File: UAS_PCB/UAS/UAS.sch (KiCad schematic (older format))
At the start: 18 parts, among them J1 SM04B-GHS-TB(LF)(SN)-, J2 SM07B-GHS-TB(LF)(SN), J3 SM04B-GHS-TB(LF)(SN)-, J4 SM08B-GHS-TB(LF)(SN), J5 SM08B-GHS-TB(LF)(SN), J6 SM04B-GHS-TB(LF)(SN)-, J7 SM04B-GHS-TB(LF)(SN)-, J8 SM07B-GHS-TB(LF)(SN), U10 UAS-rescue_7.5V-2.4A-Converte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, U11 JST-3-Pin, U12 Signal-Pad, U13 Signal-Pad, U2 5A-5V-Converter, U3 500mA-5V-Converter, U4 12V-StepUp-Converter, U5 TB6612FNG-Dual-Motor-Driver, U7 UAS-rescue_JST-4-Pin-UAS-cache, U9 JST-3-Pin

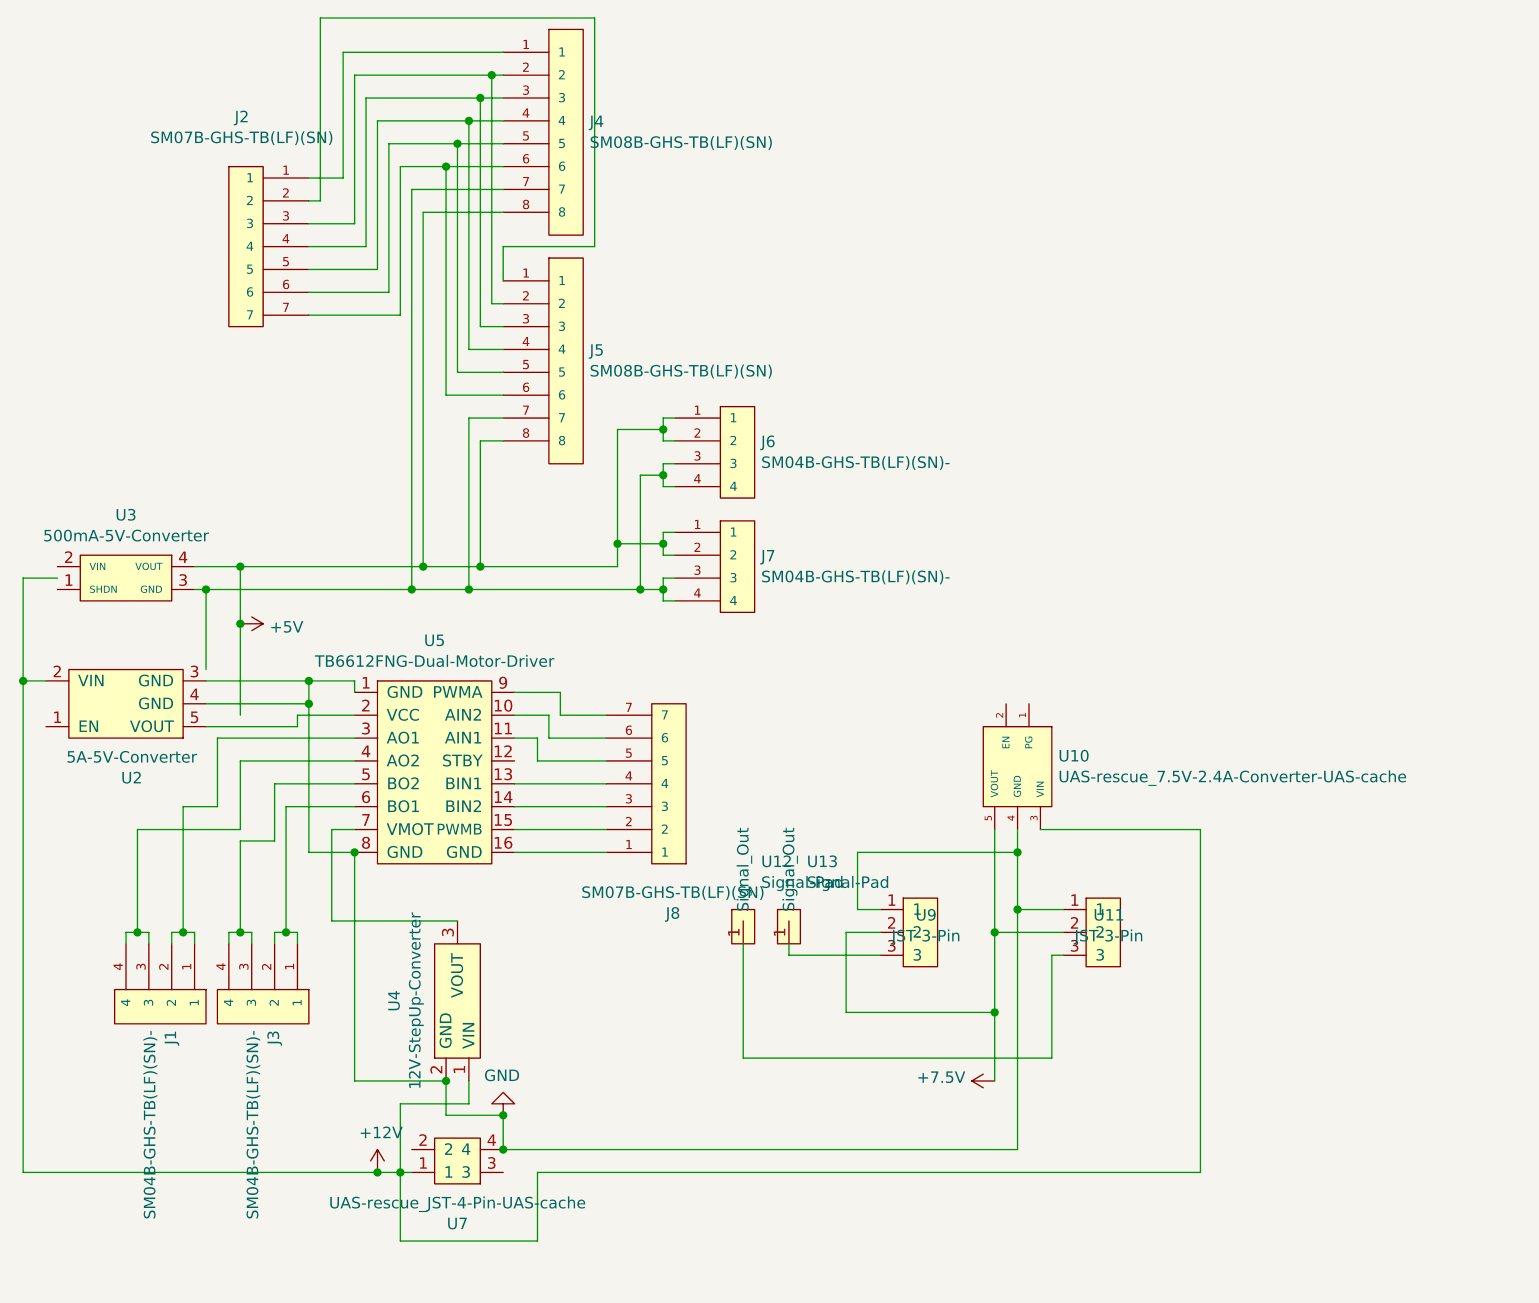
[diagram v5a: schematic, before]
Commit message: 12V Converter Added
read title
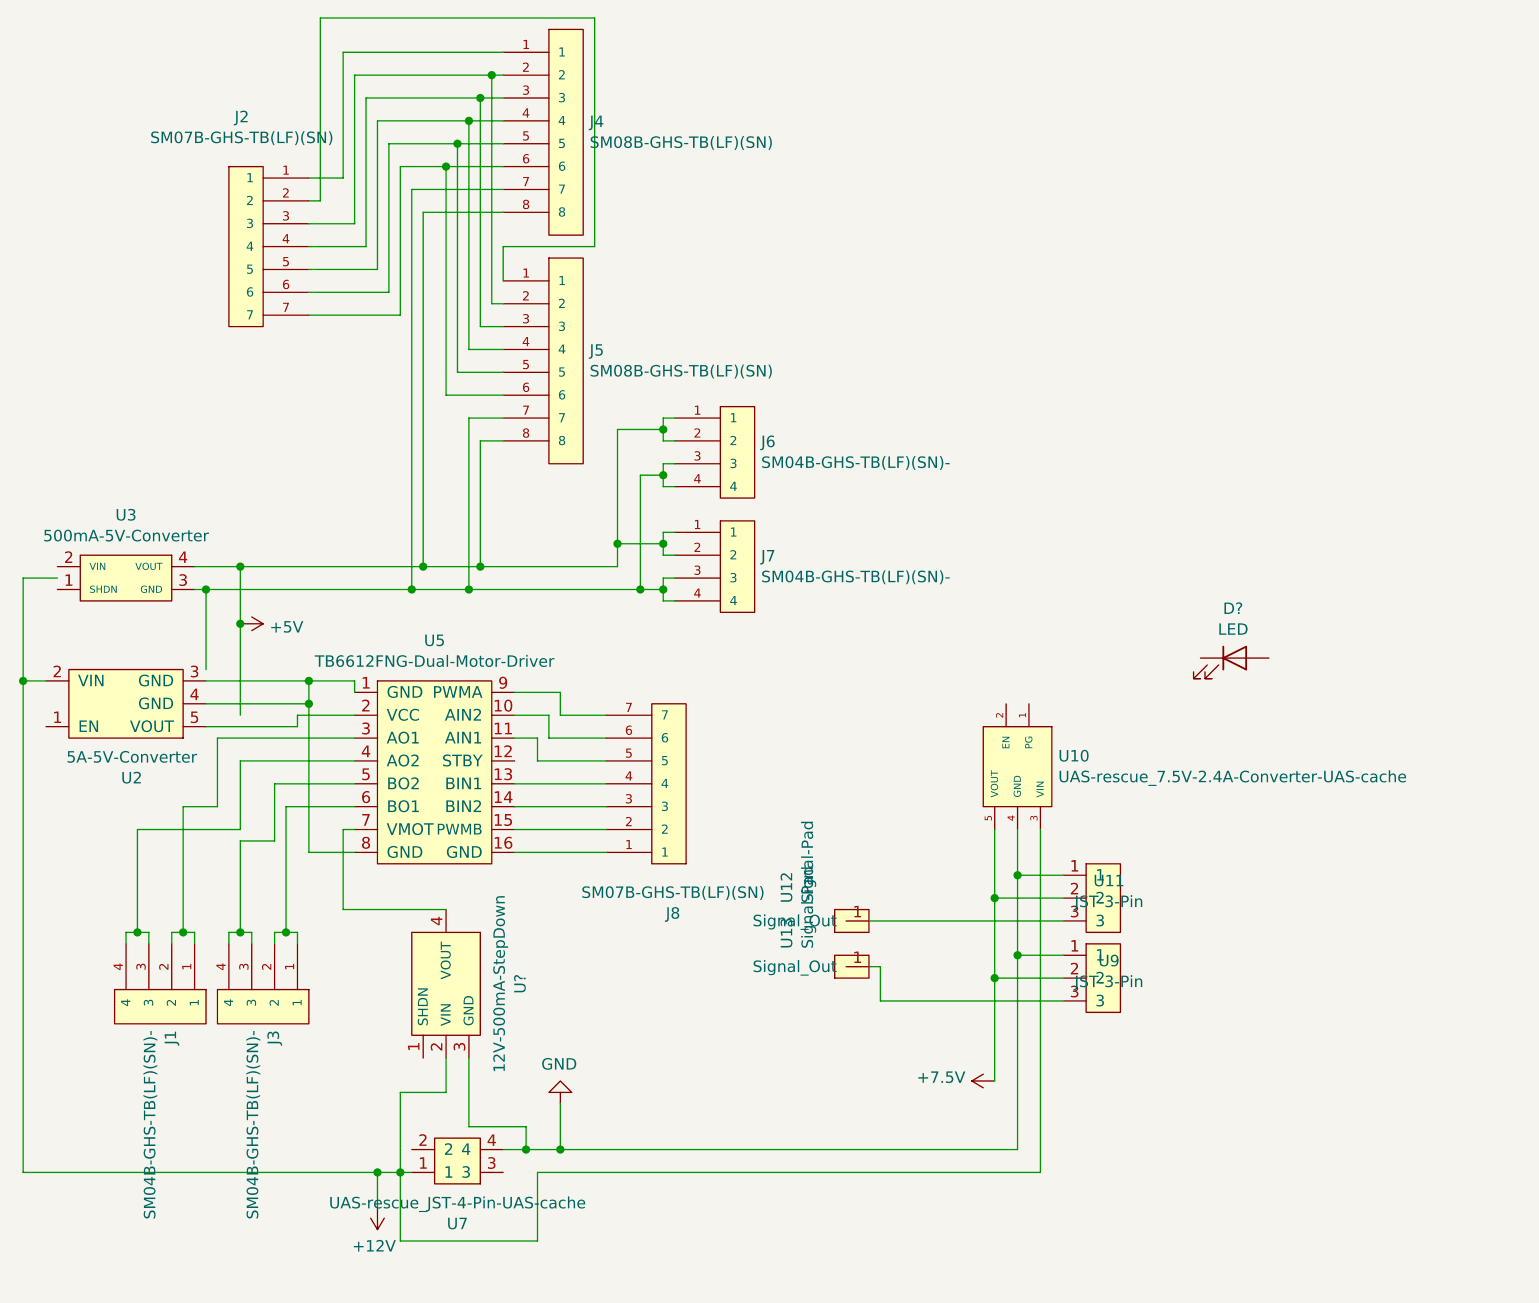
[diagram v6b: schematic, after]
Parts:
- removed U4: 12V-StepUp-Converter, UAS:Pololu_12V_Step_Up_Voltage_Regulator_SMT, symbol UAS-rescue:12V-StepUp-Converter-UAS-cache
- added D?: LED, UAS:Indicator-LED, symbol Device:LED
- added U?: 12V-500mA-StepDown, UAS:12V-500mA-StepDown, symbol UAS:12V-500mA-StepDown
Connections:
- net +12V: now also U?.2 (VIN)
- net GND: now also U?.3 (GND); no longer U2.3 (GND), U2.4 (GND), U5.1 (GND), U5.8 (GND)
- net at U5.7 (VMOT): now also U?.4 (VOUT)
- new net: U2.3 (GND), U2.4 (GND), U5.1 (GND), U5.8 (GND)
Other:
- moved on the sheet: U11, U12, U13, U9
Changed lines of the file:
@@
 $EndComp
-Wire Wire Line
-	3200 6300 3200 6150
-Wire Wire Line
-	3200 6150 2950 6150
-Wire Wire Line
-	2950 6150 2950 6000
-Wire Wire Line
-	2750 6400 2750 6100
-Wire Wire Line
-	3050 6100 3050 6000
-Wire Wire Line
-	2750 6100 3050 6100
-Wire Wire Line
-	3000 5300 2450 5300
-Wire Wire Line
-	2450 5300 2450 4900
-Wire Wire Line
-	2450 4900 2550 4900
-Wire Wire Line
-	2550 5000 2550 6000
-Wire Wire Line
-	2550 6000 2950 6000
-Connection ~ 2950 6000
 Wire Wire Line
 	1100 4250 1100 6400
-Wire Wire Line
-	1100 6400 2650 6400
 Connection ~ 1100 4250
 Connection ~ 2750 6400
@@
 Wire Wire Line
 	2350 5000 2550 5000
-Connection ~ 2550 5000
-Wire Wire Line
-	6250 6400 3350 6400
 Wire Wire Line
 	3350 6400 3350 6700
@@
 	2750 6700 2750 6400
 Wire Wire Line
-	3200 6300 5450 6300
-Connection ~ 3200 6300
-$Comp
-L UAS-rescue:Signal-Pad-UAS-cache U12
-U 1 1 60391DEE
-P 4250 5300
-F 0 "U12" H 4328 5559 50  0000 L CNN
-F 1 "Signal-Pad" H 4328 5468 50  0000 L CNN
-F 2 "UAS:Individual_Solder_Pad" H 4250 5300 50  0001 C CNN
-F 3 "" H 4250 5300 50  0001 C CNN
-	1    4250 5300
-	1    0    0    -1
-$EndComp
-$Comp
-L UAS-rescue:Signal-Pad-UAS-cache U13
-U 1 1 60392D35
-P 4450 5300
-F 0 "U13" H 4528 5559 50  0000 L CNN
-F 1 "Signal-Pad" H 4528 5468 50  0000 L CNN
-F 2 "UAS:Individual_Solder_Pad" H 4450 5300 50  0001 C CNN
-F 3 "" H 4450 5300 50  0001 C CNN
-	1    4450 5300
-	1    0    0    -1
-$EndComp
+	3200 6300 3300 6300
 $Comp
 L power:GND #PWR0101
 U 1 1 6038ECCA
-P 3200 6150
-F 0 "#PWR0101" H 3200 5900 50  0001 C CNN
-F 1 "GND" H 3205 5977 50  0000 C CNN
-F 2 "" H 3200 6150 50  0001 C CNN
-F 3 "" H 3200 6150 50  0001 C CNN
-	1    3200 6150
+P 3450 6100
+F 0 "#PWR0101" H 3450 5850 50  0001 C CNN
+F 1 "GND" H 3455 5927 50  0000 C CNN
+F 2 "" H 3450 6100 50  0001 C CNN
+F 3 "" H 3450 6100 50  0001 C CNN
+	1    3450 6100
 	-1   0    0    1
 $EndComp
-Connection ~ 3200 6150
 Wire Wire Line
 	2350 4350 2350 4250
@@
 L power:+12V #PWR0102
 U 1 1 603B00E9
-P 2650 6400
-F 0 "#PWR0102" H 2650 6250 50  0001 C CNN
-F 1 "+12V" H 2665 6573 50  0000 C CNN
-F 2 "" H 2650 6400 50  0001 C CNN
-F 3 "" H 2650 6400 50  0001 C CNN
-	1    2650 6400
-	1    0    0    -1
-$EndComp
-Connection ~ 2650 6400
-Wire Wire Line
-	2650 6400 2750 6400
+P 2650 6550
+F 0 "#PWR0102" H 2650 6400 50  0001 C CNN
+F 1 "+12V" H 2665 6723 50  0000 C CNN
+F 2 "" H 2650 6550 50  0001 C CNN
+F 3 "" H 2650 6550 50  0001 C CNN
+	1    2650 6550
+	-1   0    0    1
+$EndComp
 $Comp
 L power:+5V #PWR0103
@@
 Wire Wire Line
 	3450 4300 3250 4300
-$Comp
-L UAS-rescue:12V-StepUp-Converter-UAS-cache U4
-U 1 1 60363213
-P 2800 5650
-F 0 "U4" H 2800 5726 50  0000 C CNN
-F 1 "12V-StepUp-Converter" H 2800 5635 50  0000 C CNN
-F 2 "UAS:Pololu_12V_Step_Up_Voltage_Regulator_SMT" H 2800 5750 50  0001 C CNN
-F 3 "" H 2800 5750 50  0001 C CNN
-	1    2800 5650
-	0    -1   -1   0
-$EndComp
-Wire Wire Line
-	6250 4900 6250 6400
-Wire Wire Line
-	4250 5400 4250 5900
 Wire Wire Line
 	1900 4450 2300 4450
-Wire Wire Line
-	4250 5900 5600 5900
-$Comp
-L UAS:JST-3-pin-Revised-Symbol U9
-U 1 1 6035FF82
-P 5050 5350
-F 0 "U9" H 5050 5425 50  0000 C CNN
-F 1 "JST-3-Pin" H 5050 5334 50  0000 C CNN
-F 2 "UAS:JST_SM03B-PASS-TBT(LF)(SN)" H 5050 5450 50  0001 C CNN
-F 3 "" H 5050 5450 50  0001 C CNN
-	1    5050 5350
-	1    0    0    -1
-$EndComp
-Wire Wire Line
-	4700 5350 4700 5700
-Wire Wire Line
-	4700 5700 5350 5700
-Wire Wire Line
-	4700 5350 4850 5350
-Connection ~ 5350 5700
-Wire Wire Line
-	5350 5700 5350 6000
-Wire Wire Line
-	4850 5250 4750 5250
-Wire Wire Line
-	4750 5250 4750 5000
-Wire Wire Line
-	5450 5000 5450 5250
-Connection ~ 5450 5000
-Wire Wire Line
-	4750 5000 5450 5000
-Wire Wire Line
-	5450 4900 5450 5000
 $Comp
 L UAS-rescue:UAS-rescue_7.5V-2.4A-Converter-UAS-cache-UAS-cache U10
@@
 	0    1    1    0
 $EndComp
-Connection ~ 5450 5250
-Wire Wire Line
-	5450 6300 5450 5250
-Wire Wire Line
-	5650 5250 5450 5250
-Connection ~ 5350 5350
-Wire Wire Line
-	5350 5350 5350 4900
-Wire Wire Line
-	5650 5350 5350 5350
-Wire Wire Line
-	5600 5450 5600 5900
-Wire Wire Line
-	5600 5450 5650 5450
+$Comp
+L UAS:JST-3-pin-Revised-Symbol U9
+U 1 1 6035FF82
+P 5850 5550
+F 0 "U9" H 5850 5625 50  0000 C CNN
+F 1 "JST-3-Pin" H 5850 5534 50  0000 C CNN
+F 2 "UAS:JST_SM03B-PASS-TBT(LF)(SN)" H 5850 5650 50  0001 C CNN
+F 3 "" H 5850 5650 50  0001 C CNN
+	1    5850 5550
+	1    0    0    -1
+$EndComp
 $Comp
 L UAS:JST-3-pin-Revised-Symbol U11
 U 1 1 60369E43
-P 5850 5350
-F 0 "U11" H 5850 5425 50  0000 C CNN
-F 1 "JST-3-Pin" H 5850 5334 50  0000 C CNN
-F 2 "UAS:JST_SM03B-PASS-TBT(LF)(SN)" H 5850 5450 50  0001 C CNN
-F 3 "" H 5850 5450 50  0001 C CNN
-	1    5850 5350
-	1    0    0    -1
-$EndComp
-Wire Wire Line
-	5550 4900 6250 4900
-Wire Wire Line
-	5350 5350 5350 5700
-Wire Wire Line
-	4850 5450 4450 5450
-Wire Wire Line
-	4450 5450 4450 5400
+P 5850 5200
+F 0 "U11" H 5850 5275 50  0000 C CNN
+F 1 "JST-3-Pin" H 5850 5184 50  0000 C CNN
+F 2 "UAS:JST_SM03B-PASS-TBT(LF)(SN)" H 5850 5300 50  0001 C CNN
+F 3 "" H 5850 5300 50  0001 C CNN
+	1    5850 5200
+	1    0    0    -1
+$EndComp
+Wire Wire Line
+	5650 5100 5450 5100
+Wire Wire Line
+	5450 4900 5450 5100
+Connection ~ 5450 5100
+Wire Wire Line
+	5650 5450 5450 5450
+Wire Wire Line
+	5450 5100 5450 5450
+Wire Wire Line
+	5450 5450 5450 6300
+Connection ~ 5450 5450
+Wire Wire Line
+	5550 4900 5550 6400
+Wire Wire Line
+	5550 6400 3350 6400
+Wire Wire Line
+	5650 5200 5350 5200
+Wire Wire Line
+	5350 4900 5350 5200
+Connection ~ 5350 5200
+Wire Wire Line
+	5650 5550 5350 5550
+Wire Wire Line
+	5350 5200 5350 5550
+Wire Wire Line
+	5350 5550 5350 6000
+Connection ~ 5350 5550
+$Comp
+L UAS-rescue:Signal-Pad-UAS-cache U13
+U 1 1 60392D35
+P 4700 5500
+F 0 "U13" H 4778 5759 50  0000 L CNN
+F 1 "Signal-Pad" H 4778 5668 50  0000 L CNN
+F 2 "UAS:Individual_Solder_Pad" H 4700 5500 50  0001 C CNN
+F 3 "" H 4700 5500 50  0001 C CNN
+	1    4700 5500
+	0    -1   -1   0
+$EndComp
+$Comp
+L UAS-rescue:Signal-Pad-UAS-cache U12
+U 1 1 60391DEE
+P 4700 5300
+F 0 "U12" H 4778 5559 50  0000 L CNN
+F 1 "Signal-Pad" H 4778 5468 50  0000 L CNN
+F 2 "UAS:Individual_Solder_Pad" H 4700 5300 50  0001 C CNN
+F 3 "" H 4700 5300 50  0001 C CNN
+	1    4700 5300
+	0    -1   -1   0
+$EndComp
+Wire Wire Line
+	5650 5300 4800 5300
+Wire Wire Line
+	4850 5650 4850 5500
+Wire Wire Line
+	4850 5500 4800 5500
+Wire Wire Line
+	4850 5650 5650 5650
+$Comp
+L Device:LED D?
+U 1 1 60925126
+P 6400 4150
+F 0 "D?" H 6393 4366 50  0000 C CNN
+F 1 "LED" H 6393 4275 50  0000 C CNN
+F 2 "UAS:Indicator-LED" H 6400 4150 50  0001 C CNN
+F 3 "~" H 6400 4150 50  0001 C CNN
+	1    6400 4150
+	1    0    0    -1
+$EndComp
+$Comp
+L UAS:12V-500mA-StepDown U?
+U 1 1 609351DD
+P 2900 5550
+F 0 "U?" H 2925 5925 50  0000 C CNN
+F 1 "12V-500mA-StepDown" H 2925 5834 50  0000 C CNN
+F 2 "UAS:12V-500mA-StepDown" H 2900 5950 50  0001 C CNN
+F 3 "" H 2900 5950 50  0001 C CNN
+	1    2900 5550
+	0    1    1    0
+$EndComp
+Wire Wire Line
+	2950 5250 2500 5250
+Wire Wire Line
+	2500 5250 2500 4900
+Wire Wire Line
+	2500 4900 2550 4900
+Wire Wire Line
+	1100 6400 2650 6400
+Wire Wire Line
+	2650 6550 2650 6400
+Connection ~ 2650 6400
+Wire Wire Line
+	2650 6400 2750 6400
+Wire Wire Line
+	3450 6100 3450 6300
+Connection ~ 3450 6300
+Wire Wire Line
+	3450 6300 5450 6300
+Wire Wire Line
+	3050 5900 3050 6200
+Wire Wire Line
+	3050 6200 3300 6200
+Wire Wire Line
+	3300 6200 3300 6300
+Connection ~ 3300 6300
+Wire Wire Line
+	3300 6300 3450 6300
+Wire Wire Line
+	2950 5900 2950 6050
+Wire Wire Line
+	2950 6050 2750 6050
+Wire Wire Line
+	2750 6050 2750 6400
 $EndSCHEMATC

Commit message: Indicator LED and Wiring
I push too often but #grindGithubCommits
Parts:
- gave numbers to parts that had none: 2
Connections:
- net +5V: now also D1.2 (A); no longer J4.8, J5.8, J6.1, J6.2, J7.1, J7.2
- net at J4.7, J5.7, J6.3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: now also D1.1 (K)
- new net: J4.8, J5.8, J6.1, J6.2, J7.1, J7.2
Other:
- moved on the sheet: D1
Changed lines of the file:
@@
 $EndComp
-Wire Wire Line
-	1250 3800 1100 3800
-Wire Wire Line
-	1100 3800 1100 4250
 Wire Wire Line
 	1100 4250 1200 4250
@@
 	-1   0    0    1
 $EndComp
-Wire Wire Line
-	1100 4250 1100 6400
-Connection ~ 1100 4250
 Connection ~ 2750 6400
 Wire Wire Line
@@
 	3900 3800 3900 3850
 Wire Wire Line
-	2050 3750 2850 3750
-Wire Wire Line
 	3700 3750 3700 3650
 Wire Wire Line
 	3700 3650 3900 3650
-Connection ~ 2050 3750
 Connection ~ 3900 3650
 Wire Wire Line
@@
 	3200 2100 2800 2100
 Wire Wire Line
-	2800 2100 2800 3850
+	2800 2100 2800 3750
 Connection ~ 2800 3850
 Wire Wire Line
@@
 Wire Wire Line
 	2850 2200 2850 3750
-Connection ~ 2850 3750
 Wire Wire Line
 	2850 3750 3100 3750
@@
 	4850 5650 5650 5650
 $Comp
-L Device:LED D?
-U 1 1 60925126
-P 6400 4150
-F 0 "D?" H 6393 4366 50  0000 C CNN
-F 1 "LED" H 6393 4275 50  0000 C CNN
-F 2 "UAS:Indicator-LED" H 6400 4150 50  0001 C CNN
-F 3 "~" H 6400 4150 50  0001 C CNN
-	1    6400 4150
-	1    0    0    -1
-$EndComp
-$Comp
-L UAS:12V-500mA-StepDown U?
+L UAS:12V-500mA-StepDown U1
 U 1 1 609351DD
 P 2900 5550
-F 0 "U?" H 2925 5925 50  0000 C CNN
+F 0 "U1" H 2925 5925 50  0000 C CNN
 F 1 "12V-500mA-StepDown" H 2925 5834 50  0000 C CNN
 F 2 "UAS:12V-500mA-StepDown" H 2900 5950 50  0001 C CNN
@@
 	2500 4900 2550 4900
 Wire Wire Line
-	1100 6400 2650 6400
-Wire Wire Line
 	2650 6550 2650 6400
-Connection ~ 2650 6400
 Wire Wire Line
 	2650 6400 2750 6400
@@
 Wire Wire Line
 	2750 6050 2750 6400
+Connection ~ 2650 6400
+Wire Wire Line
+	1100 6400 2650 6400
+Wire Wire Line
+	1100 4250 1100 6400
+Connection ~ 1100 4250
+Wire Wire Line
+	1100 3800 1100 4250
+Wire Wire Line
+	1250 3800 1100 3800
+$Comp
+L Device:LED D1
+U 1 1 60925126
+P 2450 3750
+F 0 "D1" H 2443 3966 50  0000 C CNN
+F 1 "LED" H 2443 3875 50  0000 C CNN
+F 2 "UAS:Indicator-LED" H 2450 3750 50  0001 C CNN
+F 3 "~" H 2450 3750 50  0001 C CNN
+	1    2450 3750
+	-1   0    0    1
+$EndComp
+Wire Wire Line
+	2300 3750 2050 3750
+Connection ~ 2050 3750
+Wire Wire Line
+	2600 3750 2800 3750
+Connection ~ 2800 3750
+Wire Wire Line
+	2800 3750 2800 3850
 $EndSCHEMATC
